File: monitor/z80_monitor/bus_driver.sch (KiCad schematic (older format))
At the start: 13 parts, among them J1 Conn_02x25_Odd_Even, U1 74HC237, U10 74HCT365, U11 74HC573, U12 74LS05, U2 74HCT245, U3 74HC573, U4 74LS04, U5 74HC32, U6 74LS00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

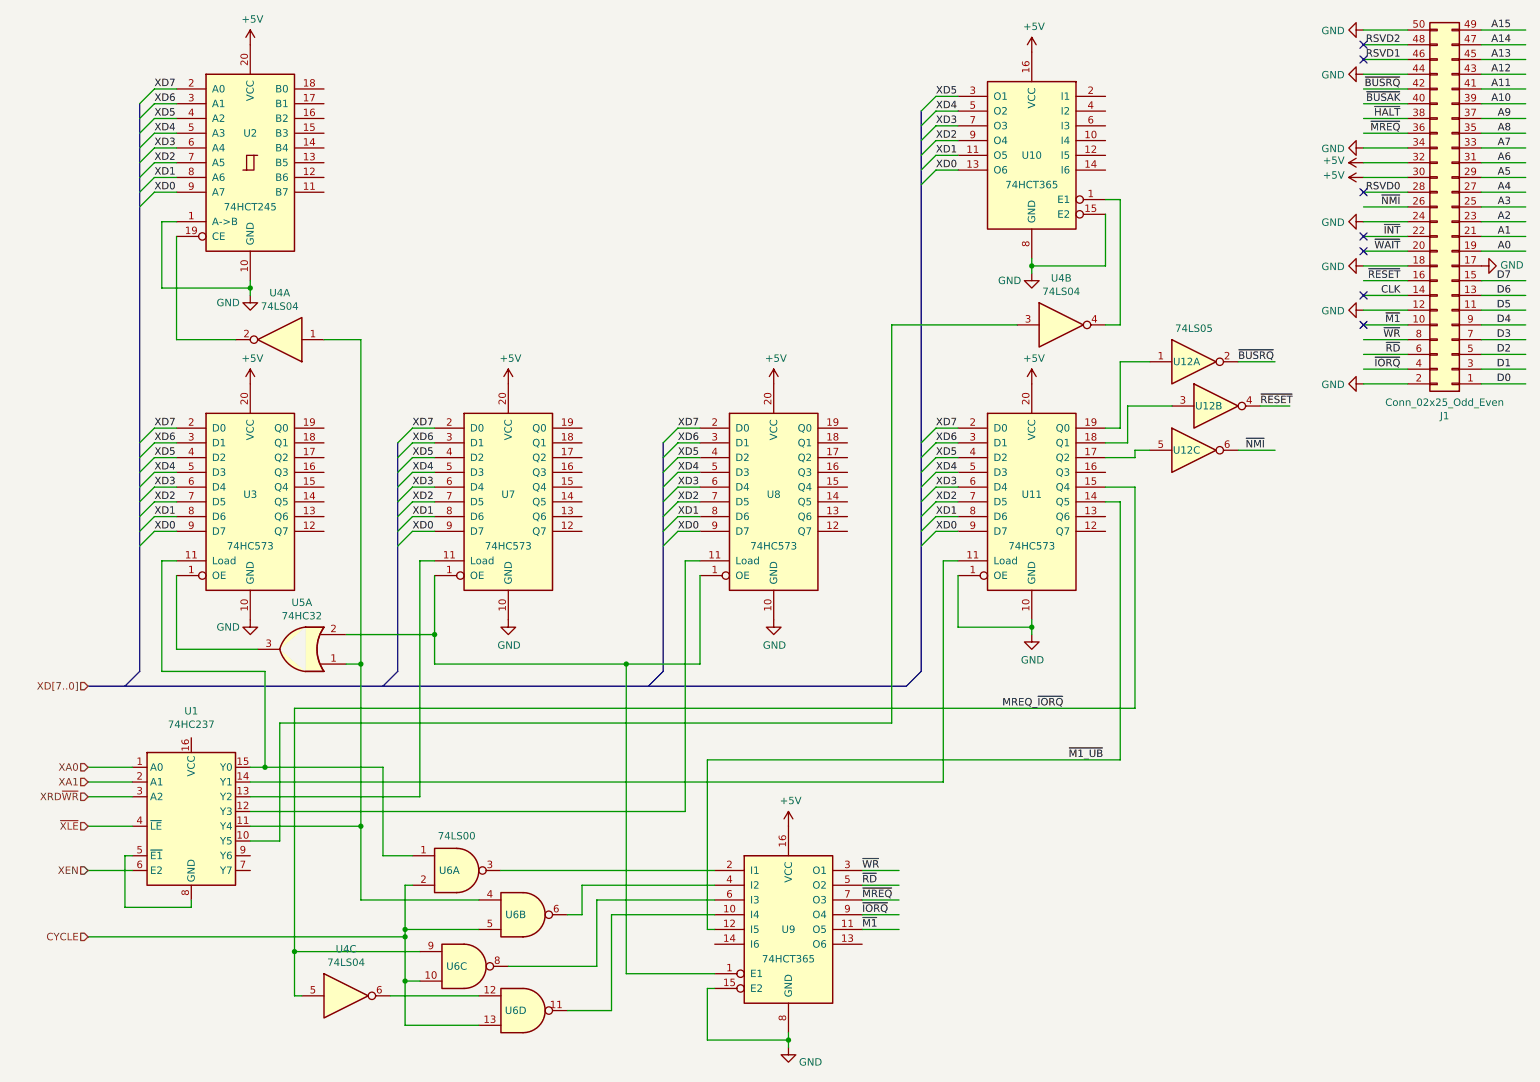
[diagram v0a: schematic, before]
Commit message: Assign some footprints and begin to play with layout
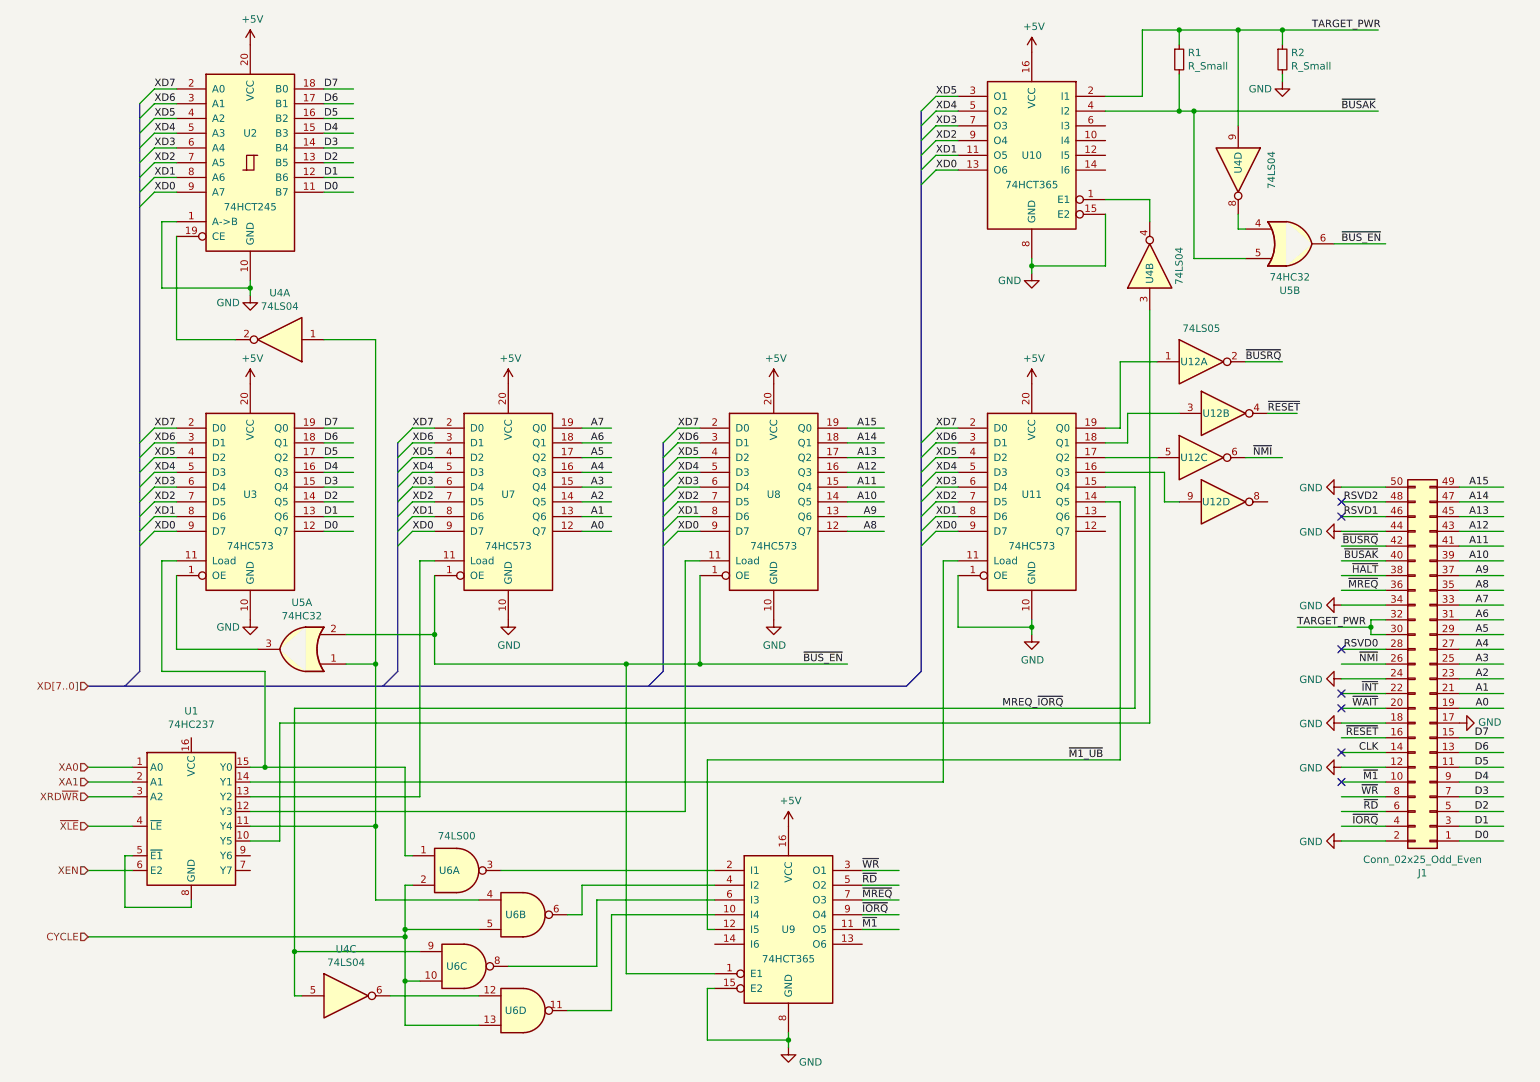
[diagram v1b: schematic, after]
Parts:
- added R1, R2: R_Small, Resistors_ThroughHole:R_Axial_DIN0411_L9.9mm_D3.6mm_P12.70mm_Horizontal, symbol Device:R_Small
- added unit 4 of U12
- added unit 4 of U4
- added unit 2 of U5
- U1, U10, U9: footprint (none) -> Housings_DIP:DIP-16_W7.62mm
- U11, U3, U7, U8: footprint (none) -> Housings_DIP:DIP-20_W7.62mm...
- U12, U4, U5, U6: footprint (none) -> Housings_DIP:DIP-14_W7.62mm
- U2: footprint (none) -> Housings_DIP:DIP-20_W7.62mm
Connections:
- net labels added: TARGET_PWR, ~BUS_EN~
- wire segments 215 -> 269
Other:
- moved on the sheet: J1, U12A, U12B, U12C, U4B

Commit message: More updates.
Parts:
- added R?: R_Small, Resistors_ThroughHole:R_Axial_DIN0411_L9.9mm_D3.6mm_P12.70mm_Horizontal, symbol Device:R_Small
- U11, U3, U7, U8: footprint Housings_DIP:DIP-20_W7.62mm... -> Housings_DIP:DIP-20_W7.62mm
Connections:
- wire segments 269 -> 274
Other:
- moved on the sheet: U4D
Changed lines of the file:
@@
 F 0 "U7" H 3950 3950 50  0000 C CNN
 F 1 "74HC573" H 3950 3600 50  0000 C CNN
-F 2 "Housings_DIP:DIP-20_W7.62mm..." H 3950 3900 50  0001 C CNN
+F 2 "Housings_DIP:DIP-20_W7.62mm" H 3950 3900 50  0001 C CNN
 F 3 "" H 3950 3900 50  0001 C CNN
 	1    3950 3900
@@
 F 0 "U11" H 7500 3950 50  0000 C CNN
 F 1 "74HC573" H 7500 3600 50  0000 C CNN
-F 2 "Housings_DIP:DIP-20_W7.62mm..." H 7500 3900 50  0001 C CNN
+F 2 "Housings_DIP:DIP-20_W7.62mm" H 7500 3900 50  0001 C CNN
 F 3 "" H 7500 3900 50  0001 C CNN
 	1    7500 3900
@@
 F 0 "U8" H 5750 3950 50  0000 C CNN
 F 1 "74HC573" H 5750 3600 50  0000 C CNN
-F 2 "Housings_DIP:DIP-20_W7.62mm..." H 5750 3900 50  0001 C CNN
+F 2 "Housings_DIP:DIP-20_W7.62mm" H 5750 3900 50  0001 C CNN
 F 3 "" H 5750 3900 50  0001 C CNN
 	1    5750 3900
@@
 F 0 "U3" H 2200 3950 50  0000 C CNN
 F 1 "74HC573" H 2200 3600 50  0000 C CNN
-F 2 "Housings_DIP:DIP-20_W7.62mm..." H 2200 3900 50  0001 C CNN
+F 2 "Housings_DIP:DIP-20_W7.62mm" H 2200 3900 50  0001 C CNN
 F 3 "" H 2200 3900 50  0001 C CNN
 	1    2200 3900
@@
 ~BUS_EN~
 Wire Wire Line
-	8000 1150 8250 1150
+	8000 1150 8150 1150
 Wire Wire Line
 	8000 1250 8500 1250
-$Comp
-L 74xx:74LS04 U4
-U 4 1 5FE8F245
-P 8900 1650
-F 0 "U4" H 8850 1650 50  0000 C CNN
-F 1 "74LS04" H 8900 1876 50  0000 C CNN
-F 2 "Housings_DIP:DIP-14_W7.62mm" H 8900 1650 50  0001 C CNN
-F 3 "" H 8900 1650 50  0001 C CNN
-	4    8900 1650
-	0    1    1    0
-$EndComp
 $Comp
 L Device:R_Small R2
@@
 $EndComp
 Wire Wire Line
-	8250 700  8500 700
+	8150 700  8300 700
 $Comp
 L Device:R_Small R1
@@
 	8500 1250 8600 1250
 Wire Wire Line
-	8900 1350 8900 700
+	8900 1400 8900 700
 Connection ~ 8900 700
 Wire Wire Line
 	8900 700  9200 700
 Wire Wire Line
-	8250 700  8250 1150
+	8150 700  8150 1150
 Wire Wire Line
 	9200 800  9200 700
@@
 Wire Wire Line
 	8950 2050 8900 2050
-Wire Wire Line
-	8900 2050 8900 1950
 Wire Wire Line
 	8950 2250 8600 2250
@@
 Wire Wire Line
 	8400 3900 8500 3900
+Wire Wire Line
+	8900 2050 8900 2000
+$Comp
+L 74xx:74LS04 U4
+U 4 1 5FE8F245
+P 8900 1700
+F 0 "U4" H 8850 1700 50  0000 C CNN
+F 1 "74LS04" H 8900 1926 50  0000 C CNN
+F 2 "Housings_DIP:DIP-14_W7.62mm" H 8900 1700 50  0001 C CNN
+F 3 "" H 8900 1700 50  0001 C CNN
+	4    8900 1700
+	0    1    1    0
+$EndComp
+Wire Wire Line
+	8000 1350 8300 1350
+Text Label 9600 1350 0    50   ~ 0
+~HALT~
+$Comp
+L Device:R_Small R?
+U 1 1 5FD3F7AE
+P 8300 900
+F 0 "R?" H 8359 946 50  0000 L CNN
+F 1 "R_Small" H 8359 855 50  0000 L CNN
+F 2 "Resistors_ThroughHole:R_Axial_DIN0411_L9.9mm_D3.6mm_P12.70mm_Horizontal" H 8300 900 50  0001 C CNN
+F 3 "~" H 8300 900 50  0001 C CNN
+	1    8300 900
+	1    0    0    -1
+$EndComp
+Wire Wire Line
+	8300 1000 8300 1350
+Connection ~ 8300 1350
+Wire Wire Line
+	8300 1350 9850 1350
+Wire Wire Line
+	8300 800  8300 700
 Wire Bus Line
 	1100 5150 6650 5150
@@
 Wire Bus Line
 	1450 1200 1450 5050
+Connection ~ 8300 700
+Wire Wire Line
+	8300 700  8500 700
 $EndSCHEMATC
